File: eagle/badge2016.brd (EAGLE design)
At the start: 135 x 100.5 mm, 89 parts, among them IC1 25AA080SN, IC3 24AA01SN, J1 USB-MICRO, Q1_32.768KHZ NX5032G, Q2 BC857ALT1SMD, Q2_24MHZ NX5032G, X1 PASSER-07, X2 PASSER-07, X3 PASSER-07

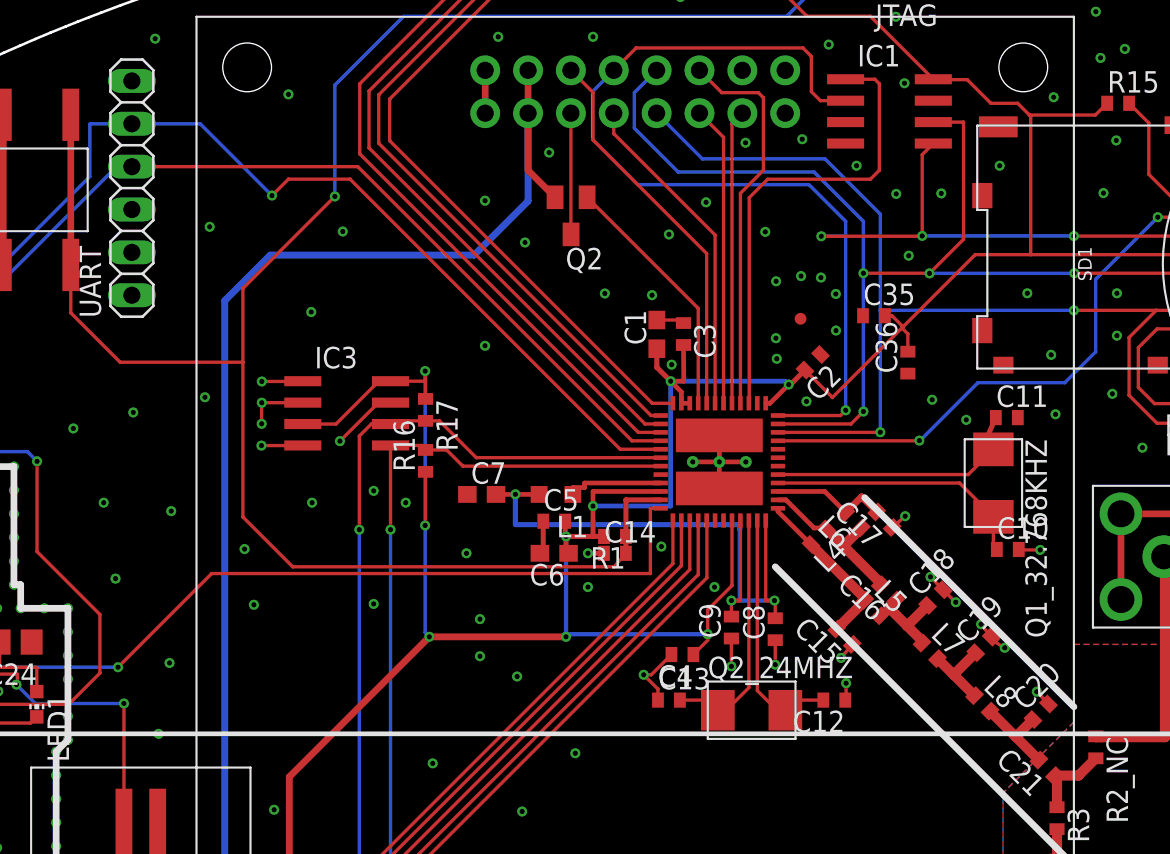
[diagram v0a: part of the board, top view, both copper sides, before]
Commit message: fixed the inductor label (nF to nH) swapped 32khz crystal to different package + added package to lbr add pinhead to battery connector
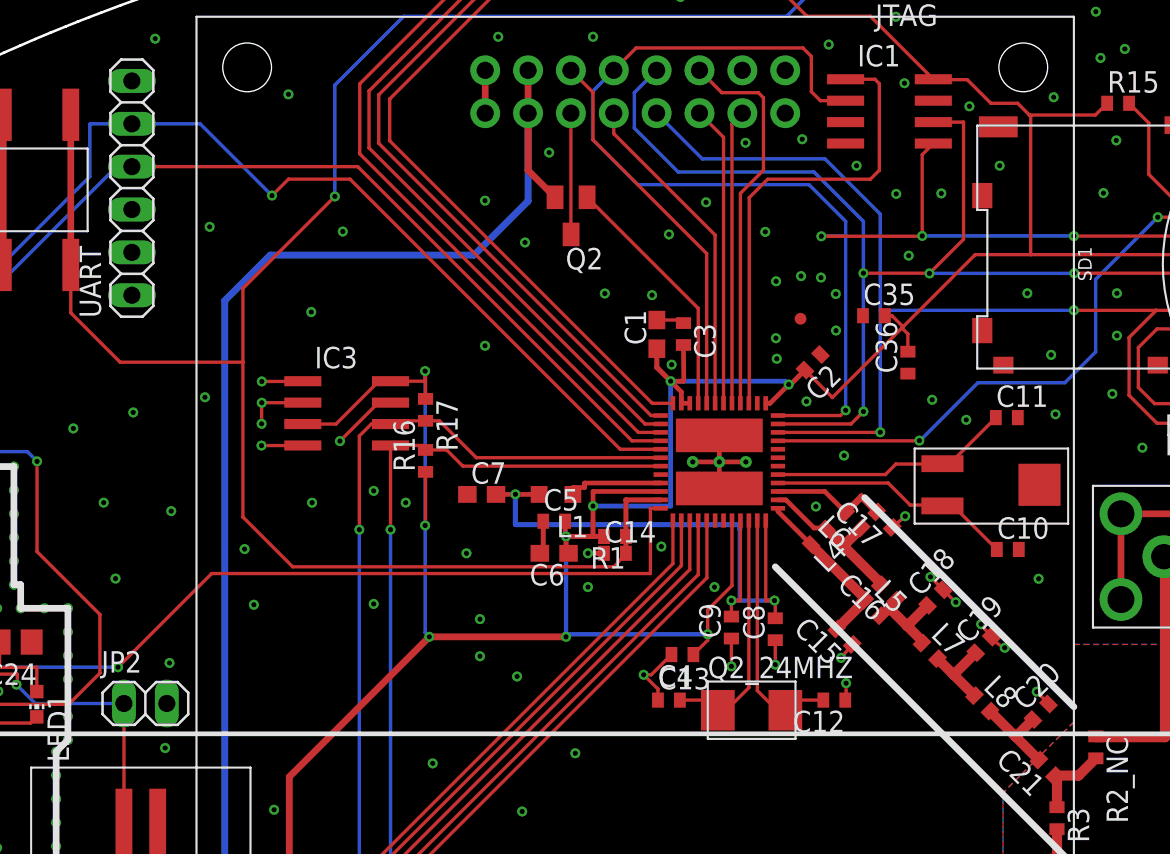
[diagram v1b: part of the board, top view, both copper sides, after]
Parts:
- removed Q1_32.768KHZ: NX5032G, ERNW_parts:NX5032G*
- added JP2: (no value), pinhead:1X02
- added U$2: 32.768Hz, ERNW_parts:CMR200T
- L1: value 6.8nF -> 6.8nH
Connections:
- removed net N$1: C11.1, Q1_32.768KHZ.1, U$1.5
- new net N$16: C11.1, U$1.5, U$2.X2
- net GND: now also JP2.2
- net N$2: now also U$2.X1; no longer Q1_32.768KHZ.2
- net N$20: now also JP2.1
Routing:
- net N$1: track 16.1 -> 0.00 mm
- net N$16: track 0.00 -> 14.3 mm
- net GND: track 195.8 -> 194.5 mm, vias 288 -> 291
- net N$2: track 15.6 -> 14.6 mm
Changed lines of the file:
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@@
 <element name="C8" library="rcl" package="C0402" value="100nF" x="84.8" y="53.2" rot="R90"/>
 <element name="C9" library="rcl" package="C0402" value="100nF" x="82.2" y="53.3" rot="R90"/>
-<element name="L1" library="rcl" package="L2012C" value="6.8nF" x="71.80685625" y="61.1893375" rot="R180"/>
+<element name="L1" library="rcl" package="L2012C" value="6.8nH" x="71.80685625" y="61.1893375" rot="R180"/>
 <element name="U$1" library="ERNW_parts" package="S-PVQFN-N48" value="CC1310" x="81.485934375" y="63.11615" rot="R180"/>
-<element name="Q1_32.768KHZ" library="ERNW_parts" package="NX5032G*" value="NX5032G" x="97.729140625" y="61.761521875" rot="R270"/>
 <element name="Q2_24MHZ" library="ERNW_parts" package="NX5032G*" value="NX5032G" x="83.5" y="48.4"/>
 <element name="JTAG" library="pinhead" package="2X05" value="" x="88.085" y="93.4" rot="R180"/>
@@
 <element name="R18" library="rcl" package="R0402" value="NC" x="110.33" y="66.57" rot="R180"/>
 <element name="R21" library="rcl" package="R0402" value="NC" x="110.34" y="65.41" rot="R180"/>
+<element name="U$2" library="ERNW_parts" package="CMR200T" value="32.768Hz" x="94.71" y="61.76" rot="R180"/>
+<element name="JP2" library="pinhead" package="1X02" value="" x="47.47" y="48.8"/>
 </elements>
 <signals>
@@
 <contactref element="C8" pad="1"/>
 <contactref element="C9" pad="1"/>
-<contactref element="C11" pad="2"/>
-<contactref element="C10" pad="2"/>
 <contactref element="C12" pad="1"/>
 <contactref element="C13" pad="1"/>
@@
 <via x="94" y="56.3" extent="1-16" drill="0.3"/>
 <via x="92.5" y="59.9" extent="1-16" drill="0.3"/>
-<via x="100.5" y="57.9" extent="1-16" drill="0.3"/>
 <via x="88.7" y="51.5" extent="1-16" drill="0.3"/>
-<wire x1="99.233878125" y1="57.927028125" x2="99.233878125" y2="57.9" width="0.2" layer="1"/>
-<wire x1="99.233878125" y1="57.9" x2="100.5" y2="57.9" width="0.2" layer="1"/>
 <wire x1="91.73190625" y1="59.23413125" x2="92.5" y2="59.9" width="0.2" layer="1"/>
 <wire x1="94" y1="56.3" x2="94.751253125" y2="55.53596875" width="0.2" layer="1"/>
@@
 <via x="46.75" y="66.05" extent="1-16" drill="0.3"/>
 <via x="45" y="60.7" extent="1-16" drill="0.3"/>
-<via x="48.25" y="47" extent="1-16" drill="0.3"/>
+<via x="48.64" y="46.16" extent="1-16" drill="0.3"/>
 <via x="46.05" y="37.2" extent="1-16" drill="0.3"/>
 <via x="45.7" y="27.7" extent="1-16" drill="0.3"/>
@@
 <via x="96.12" y="65.61" extent="1-16" drill="0.3"/>
 <via x="101.41" y="65.94" extent="1-16" drill="0.3"/>
+<contactref element="C11" pad="2"/>
+<contactref element="C10" pad="2"/>
+<via x="100.41" y="56.19" extent="1-16" drill="0.3"/>
+<via x="88.88" y="63.49" extent="1-16" drill="0.3"/>
+<via x="87.21" y="60.47" extent="1-16" drill="0.3"/>
+<via x="96.31" y="84.19" extent="1-16" drill="0.3"/>
+<contactref element="JP2" pad="2"/>
 </signal>
 <signal name="3V3">
@@
 <wire x1="86.805" y1="95.95" x2="88.085" y2="94.67" width="0.2" layer="16"/>
 </signal>
-<signal name="N$1">
-<contactref element="U$1" pad="5"/>
-<contactref element="Q1_32.768KHZ" pad="1"/>
-<contactref element="C11" pad="1"/>
-<wire x1="84.960934375" y1="62.36615" x2="96.23376875" y2="62.36615" width="0.2" layer="1"/>
-<wire x1="96.23376875" y1="62.36615" x2="97.729140625" y2="63.861521875" width="0.2" layer="1"/>
-<wire x1="97.876625" y1="65.741165625" x2="97.0306875" y2="63.861521875" width="0.3" layer="1"/>
-<wire x1="97.0306875" y1="63.861521875" x2="97.729140625" y2="63.861521875" width="0.3" layer="1"/>
-</signal>
 <signal name="N$2">
 <contactref element="U$1" pad="4"/>
-<contactref element="Q1_32.768KHZ" pad="2"/>
+<contactref element="U$2" pad="X1"/>
 <contactref element="C10" pad="1"/>
-<wire x1="84.960934375" y1="61.86615" x2="95.7245125" y2="61.86615" width="0.2" layer="1"/>
-<wire x1="95.7245125" y1="61.86615" x2="97.729140625" y2="59.861521875" width="0.2" layer="1"/>
-<wire x1="97.729140625" y1="59.861521875" x2="97.729140625" y2="58.131765625" width="0.2" layer="1"/>
-<wire x1="97.729140625" y1="58.131765625" x2="97.933878125" y2="57.927028125" width="0.2" layer="1"/>
+<wire x1="84.960934375" y1="61.86615" x2="91.49385" y2="61.86615" width="0.2" layer="1"/>
+<wire x1="91.49385" y1="61.86615" x2="92.8" y2="60.56" width="0.2" layer="1"/>
+<wire x1="92.8" y1="60.56" x2="94.66" y2="60.56" width="0.2" layer="1"/>
+<wire x1="94.66" y1="60.56" x2="94.71" y2="60.51" width="0.2" layer="1"/>
+<wire x1="94.71" y1="60.51" x2="95.35090625" y2="60.51" width="0.2" layer="1"/>
+<wire x1="95.35090625" y1="60.51" x2="97.933878125" y2="57.927028125" width="0.2" layer="1"/>
 </signal>
 <signal name="N$4">
@@
 <wire x1="39.88" y1="49.965" x2="39.83" y2="49.915" width="0.2" layer="1"/>
 <wire x1="39.83" y1="49.915" x2="40.945" y2="48.8" width="0.2" layer="16"/>
+<via x="46.2" y="48.8" extent="1-16" drill="0.3"/>
+<contactref element="JP2" pad="1"/>
 <wire x1="40.945" y1="48.8" x2="46.2" y2="48.8" width="0.2" layer="16"/>
-<via x="46.2" y="48.8" extent="1-16" drill="0.3"/>
 <wire x1="46.2" y1="48.8" x2="46.2" y2="41.5" width="0.2" layer="1"/>
 </signal>
@@
 <wire x1="83.26" y1="66.615215625" x2="83.235934375" y2="66.59115" width="0.2" layer="1"/>
 </signal>
+<signal name="N$16">
+<contactref element="C11" pad="1"/>
+<contactref element="U$2" pad="X2"/>
+<contactref element="U$1" pad="5"/>
+<wire x1="84.960934375" y1="62.36615" x2="91.32615" y2="62.36615" width="0.2" layer="1"/>
+<wire x1="91.32615" y1="62.36615" x2="91.95" y2="62.99" width="0.2" layer="1"/>
+<wire x1="91.95" y1="62.99" x2="94.69" y2="62.99" width="0.2" layer="1"/>
+<wire x1="94.69" y1="62.99" x2="94.71" y2="63.01" width="0.2" layer="1"/>
+<wire x1="94.71" y1="63.01" x2="95.145459375" y2="63.01" width="0.2" layer="1"/>
+<wire x1="95.145459375" y1="63.01" x2="97.876625" y2="65.741165625" width="0.2" layer="1"/>
+</signal>
 </signals>

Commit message: fixed PCB with design
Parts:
- removed C36: 4.7µF, rcl:C0402
- removed JP1: (no value), pinhead:1X03
- removed R15, R18, R21: NC, rcl:R0402
- removed R16, R17: 10k, rcl:R0402
- removed R2_NC: 0, rcl:R0402
- removed U$12: FT231X, ERNW_parts:QFN-20-4X4
- added IC2: FT231XQ, we-chip:QFN20-PAD
- added LOGO1: LOGO-S_LAYER, we-symbol:SPARK_TOP
- added NC-JP1: (no value), pinhead:1X03
- added NC-R15, NC-R18, NC-R21: NC, we-rcl:C0402
- added NC-R16, NC-R17: 10k, we-rcl:C0402
- added NC_C35: 100nF, we-rcl:C0402
- added NC_C36: 4.7µF, we-rcl:C0402
- added NC_LED2: (no value), we-opto:C0603
- added NC_R15, NC_R16, NC_R2, NC_R3: 0, we-rcl:C0603
- added NC_R5: 1k5, we-rcl:C0402
- added U$3: BB_TEST, ERNW_parts:BB_TEST
- added U$4: MESSAGE, ERNW_parts:MESSAGE
- added U$5: TR_BRAILLE, ERNW_parts:TR_BRAILLE
- added U$6: TR_PIGPEN, ERNW_parts:TR_PIGPEN
- added X10, X11, X12, X13, X14, X15, X16, X17, X18, X19, X20, X8, X9: PAD-1.27X1.27, we-rcl:PAD-1.27X1.27
- added X4, X5, X6, X7: PAD-0.5, we-rcl:PAD-0.5
- C1: device rcl:C0603 -> we-rcl:C0402
- C10, C11, C12, C13, C14, C15, C16, C17, C18, C19, C2, C20, C21, C22, C25, C26, C3, C30, C31, C32, C33, C34, C4, C5, C8, C9: device rcl:C0402 -> we-rcl:C0402
- C23, C24, C27, C28: device rcl:C0805 -> we-rcl:C0805
- C29: device rcl:C0805 -> we-rcl:C0603
- C35: value 100nF -> 2.2µF; device rcl:C0402 -> we-rcl:C0603
- C6, C7: device rcl:C0603 -> we-rcl:C0603
- L1: value 6.8nH -> 6.8µH; device rcl:L2012C -> we-rcl:C0402
- L4, L5, L6, L7, L8, L9: device ERNW_parts:C0402 -> we-rcl:C0402
- LED1: device led:CHIP-LED0603 -> we-opto:C0603
- R1, R10, R11, R12, R13, R14, R19, R2, R20, R4, R5, R6, R7, R9: device rcl:R0402 -> we-rcl:C0402
- R3: value 0 -> 100k; device rcl:R0402 -> we-rcl:C0402
- R8: value (none) -> 1k; device rcl:R0402 -> we-rcl:C0402
- moved R3 55.0 mm to (47.4, 52.3)
- moved C35 48.1 mm to (45.8, 54.3)
- moved C15 4.57 mm to (87.5, 57.1)
- moved C16 3.88 mm to (89.9, 58.9), turned to 225 degrees
- moved C22 3.53 mm to (100.2, 42.2), turned to 0 degrees
- moved L9 3.33 mm to (99.7, 39.7), turned to 90 degrees
- moved C21 2.82 mm to (99.9, 47.6), turned to 225 degrees
- moved C20 2.76 mm to (98.3, 49.9), turned to 135 degrees
- moved C19 2.71 mm to (94.4, 52.4), turned to 315 degrees
- moved L8 2.58 mm to (96.2, 51.2), turned to 225 degrees
- moved L7 2.37 mm to (93.5, 54.2), turned to 225 degrees
- moved L5 2.20 mm to (90.4, 56.7)
- moved C18 1.93 mm to (92.5, 55.9), turned to 135 degrees
- moved L6 1.75 mm to (88.1, 60.7), turned to 45 degrees
- moved C17 1.57 mm to (90.1, 60.7), turned to 225 degrees
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- renumbered IC3 to NC-IC3, JP2 to NC-JP2, JP4 to NC-JP4, JTAG to NC-JTAG, SD1 to NC-SD1, U$10 to NC-U$10, U$13 to NC-U$13, UART to NC-UART
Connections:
- new net N$1: IC2.19
- new net N$19: C1.1, U$1.23
- new net N$21: IC2.6
- new net N$24: IC2.18
- new net N$26: IC2.4
- new net N$31: IC2.5
- new net N$34: IC2.2
- new net N$35: U$1.32, X5.1
- new net N$36: U$1.31, X6.1
- new net N$38: U$1.30, X7.1
- new net N$39: IC2.16, NC_R5.1, X17.1
- new net N$40: NC_LED2.A, NC_R5.2
- new net N$41: U$11.5, X20.1
- new net SWITCH_DISP_2: C35.2, R3.2, U$11.8
- net !BCD: now also IC2.15; no longer U$12.15
- net !PWREN: now also IC2.14; no longer U$12.14
- net !SLEEP: now also IC2.7, X16.1; no longer U$12.7
- net 3V3: now also NC-JP1.1, NC-R15.1, NC-R16.1, NC-R17.1, NC-R18.1, NC-R21.1, NC_C35.2, NC_C36.2, NC_R16.1, NC_R16.2, X13.1; no longer C1.1, C35.2, C36.2, JP1.1, R15.1, R16.1, R17.1, R18.1, R21.1, U$1.23
- net BG_LIGHT: now also X19.1
- net DM: now also IC2.9; no longer U$12.9
- net DP: now also IC2.8; no longer U$12.8
- net GND: now also IC2.13, IC2.3, IC2.TP, L9.1, NC-JP1.2, NC_C35.1, NC_C36.1, NC_LED2.C, U$15.2, X11.1; no longer C36.1, JP1.2, L9.2, U$11.5, U$12.13, U$12.3, U$12.PAD, U$15.1
- net I2C_SCL: now also NC-R17.2, U$1.28; no longer R17.2, U$1.30
- net I2C_SDA: now also NC-R16.2, U$1.29; no longer R16.2, U$1.31
- net LED_A: now also X18.1
- net N$10: now also L6.1; no longer L6.2
- net N$11: now also L7.1, L8.2; no longer L7.2, L8.1
- net N$13: now also L8.1; no longer L8.2
- net N$14: now also U$1.6, X4.1; no longer C21.1, R2_NC.2, R3.1
- net N$15: now also C21.1, NC_R2.2, NC_R3.1, NC_R3.2; no longer R3.2
- net N$17: now also NC_R2.1; no longer R2_NC.1
- net N$20: now also U$15.1; no longer U$15.2
- net N$25: now also X8.1
- net N$32: now also X9.1
- net N$37: now also IC2.10, IC2.11, IC2.20; no longer U$12.10, U$12.11, U$12.20
- net N$6: now also L4.2, L6.2; no longer L4.1, L6.1
- net N$7: now also L4.1, L5.2; no longer L4.2, L5.1
- net N$8: now also L5.1, L7.2; no longer L5.2, L7.1
- net PCB_ANTENNA: now also L9.2; no longer L9.1
- net PROG: now also X15.1
- net RXD: now also IC2.1, U$1.7; no longer U$1.29, U$12.1
- net SD_D1: now also NC-R18.2; no longer R18.2
- net SD_D2: now also NC-R15.2; no longer R15.2
- net SPI_MISO: now also NC-R21.2; no longer R21.2
- net SWITCH_DISP: now also R3.1; no longer U$11.8
- net TXD: now also IC2.17, U$1.8; no longer U$1.28, U$12.17
- net VDDR: now also X14.1
- net VUSB_IN: now also IC2.12, X10.1; no longer U$12.12
- net V_DISP: now also NC-JP1.3, NC_R15.1, NC_R15.2, X12.1; no longer JP1.3
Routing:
- net GND: track 194.5 -> 224.3 mm, vias 291 -> 348
- net SWITCH_DISP: track 55.9 -> 36.1 mm, vias 3 -> 0
- net SWITCH_DISP_2: track 0.00 -> 19.3 mm, vias 0 -> 2
- net N$51: track 0.00 -> 14.9 mm
- net TXD: track 84.2 -> 98.5 mm, vias 1 -> 3
- net N$46: track 0.00 -> 12.7 mm
- net N$49: track 0.00 -> 12.5 mm
- net N$43: track 0.00 -> 12.4 mm
- net N$52: track 0.00 -> 12.3 mm
- net RXD: track 78.9 -> 90.8 mm, vias 2 -> 4
- net N$47: track 0.00 -> 11.8 mm
- net N$42: track 0.00 -> 11.8 mm
- net N$48: track 0.00 -> 11.7 mm
- net N$50: track 0.00 -> 6.02 mm
- net 3V3: track 280.4 -> 285.7 mm
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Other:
- board text added: "!RST"
- board text added: "!Sleep"
- board text added: "+"
- board text added: "-"
- board text added: "3v3"
- board text added: "DM"
- board text added: "DP"
- board text added: "GND"
- board text added: "I2C Flash"
- board text added: "JTAG"
- board text added: "MicroSD"
- board text added: "NC"
- board text added: "OnBoard Antenna"
- board text added: "PROG"
- board text added: "RESET"
- board text added: "RXD"
- board text added: "SMA Antenna"
- board text added: "S_DISP"
- board text added: "T R O O P E R S 1 6"
- board text added: "TCK"
- board text added: "TDI"
- board text added: "TDO"
- board text added: "TMS"
- board text added: "TROOPERS 2016"
- board text added: "TXD"
- board text added: "UART"
- board text added: "VDDR"
- board text added: "VUSB"
- board text added: "V_DISP"
- board text added: "make the world a safer place"

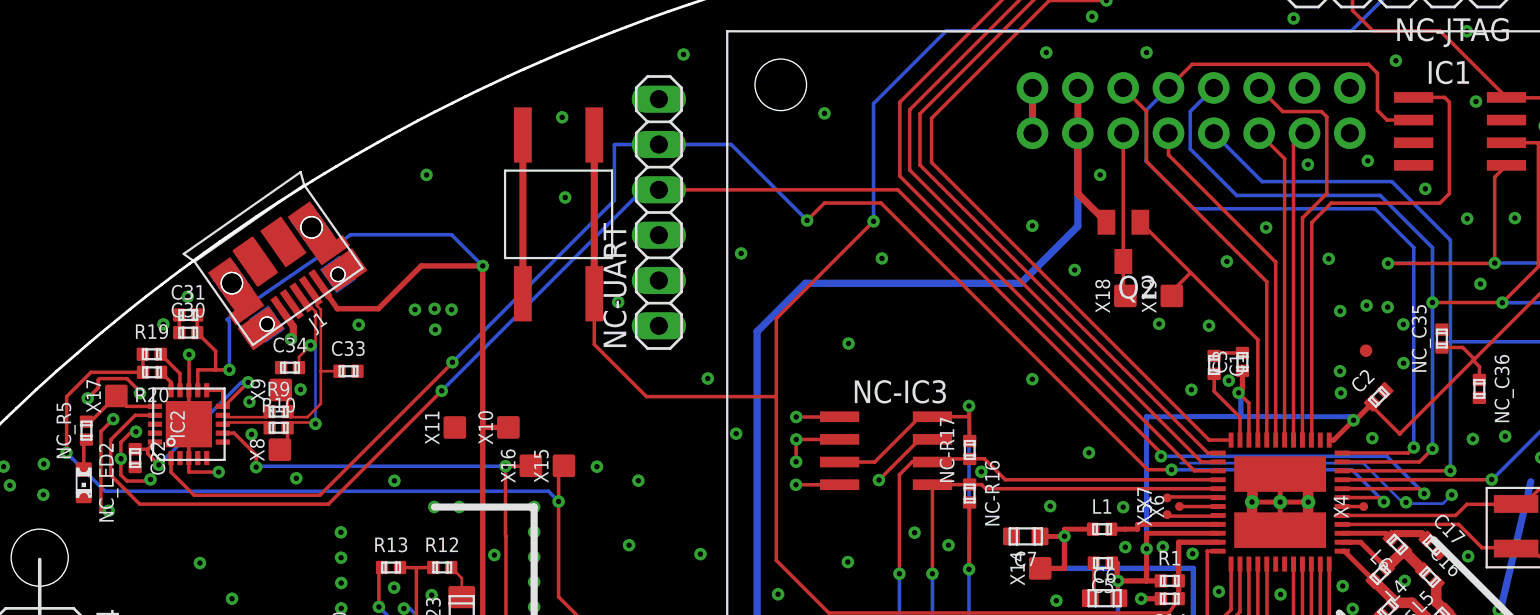
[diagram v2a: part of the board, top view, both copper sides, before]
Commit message: Update badge2016.brd
Change RX <-> TX for UART
Add additional "pin" for DIO_8
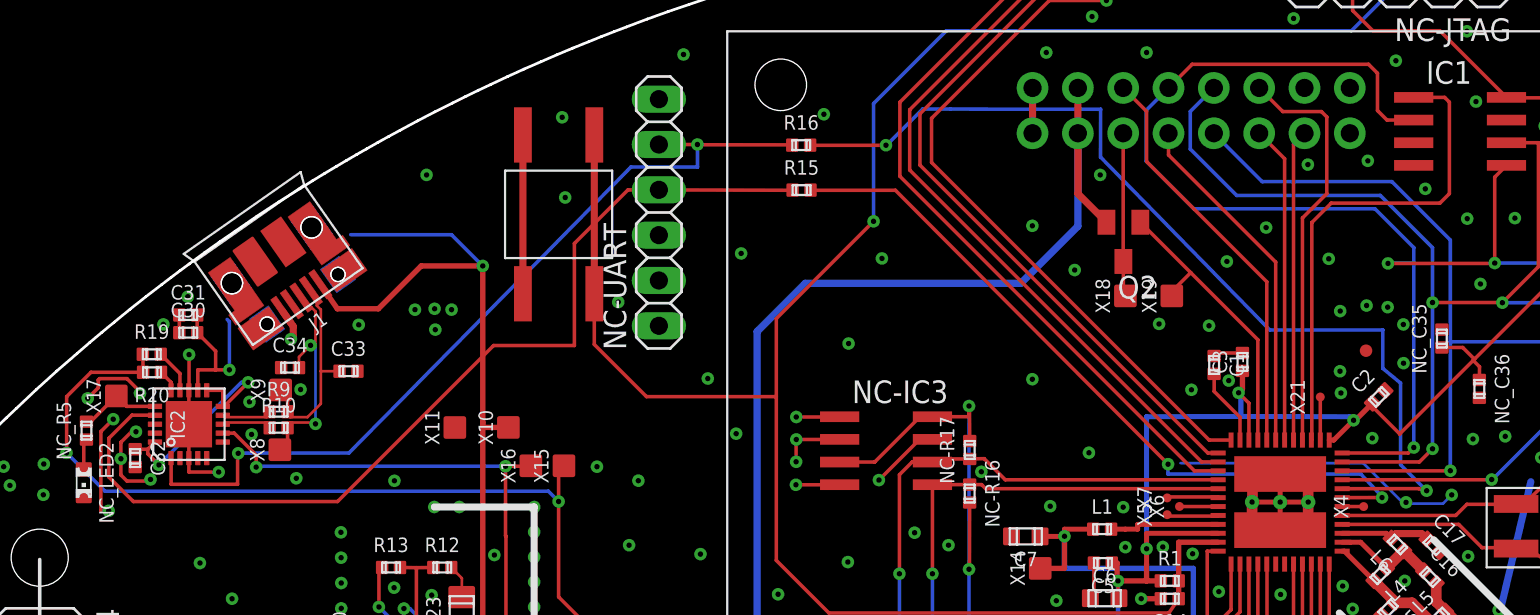
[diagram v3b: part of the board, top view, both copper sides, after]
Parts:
- added R15, R16: 0, we-rcl:C0402
- added X21: PAD-0.5, we-rcl:PAD-0.5
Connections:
- new net N$53: U$1.14, X21.1
- new net UART_RXD: R15.1, U$1.7
- new net UART_TXD: R16.1, U$1.8
- net RXD: now also R16.2; no longer U$1.7
- net TXD: now also R15.2; no longer U$1.8
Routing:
- net UART_TXD: track 0.00 -> 54.4 mm, vias 0 -> 2
- net TXD: track 98.5 -> 54.8 mm, vias 3 -> 0
- net RXD: track 90.8 -> 48.2 mm, vias 4 -> 2
- net UART_RXD: track 0.00 -> 41.7 mm, vias 0 -> 2
- net VUSB_IN: track 64.8 -> 56.4 mm
- net N$53: track 0.00 -> 2.41 mm
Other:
- board text added: "BAT+"
